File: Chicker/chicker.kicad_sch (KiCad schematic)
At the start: 0 parts

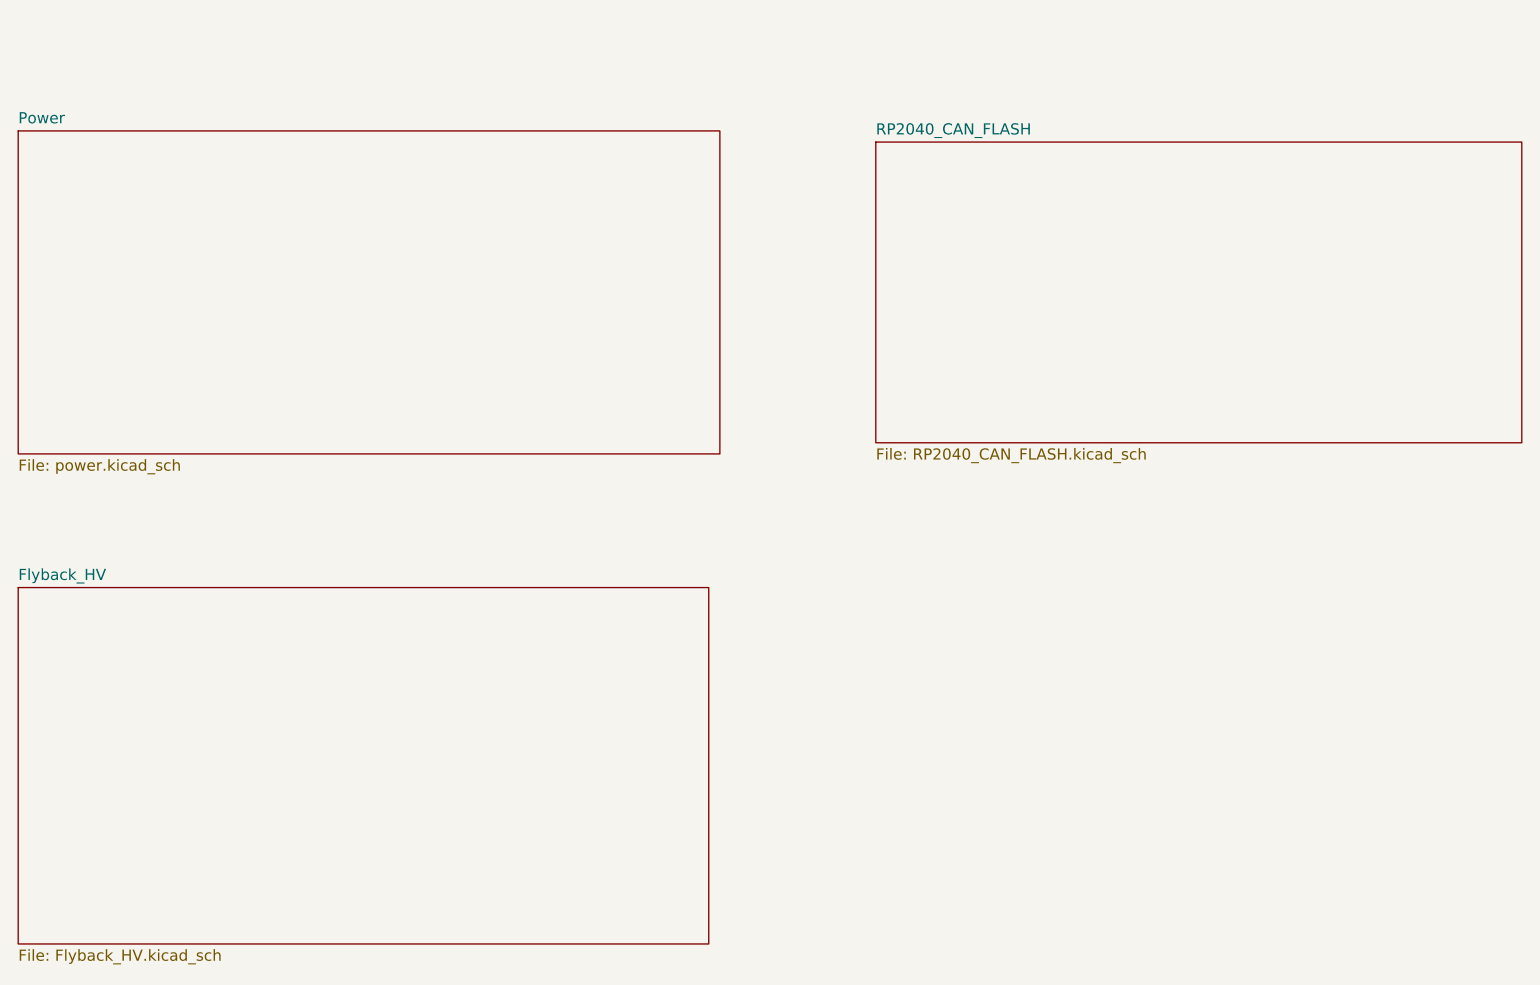
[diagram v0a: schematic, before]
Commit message: update to schematic but something on layout is broken
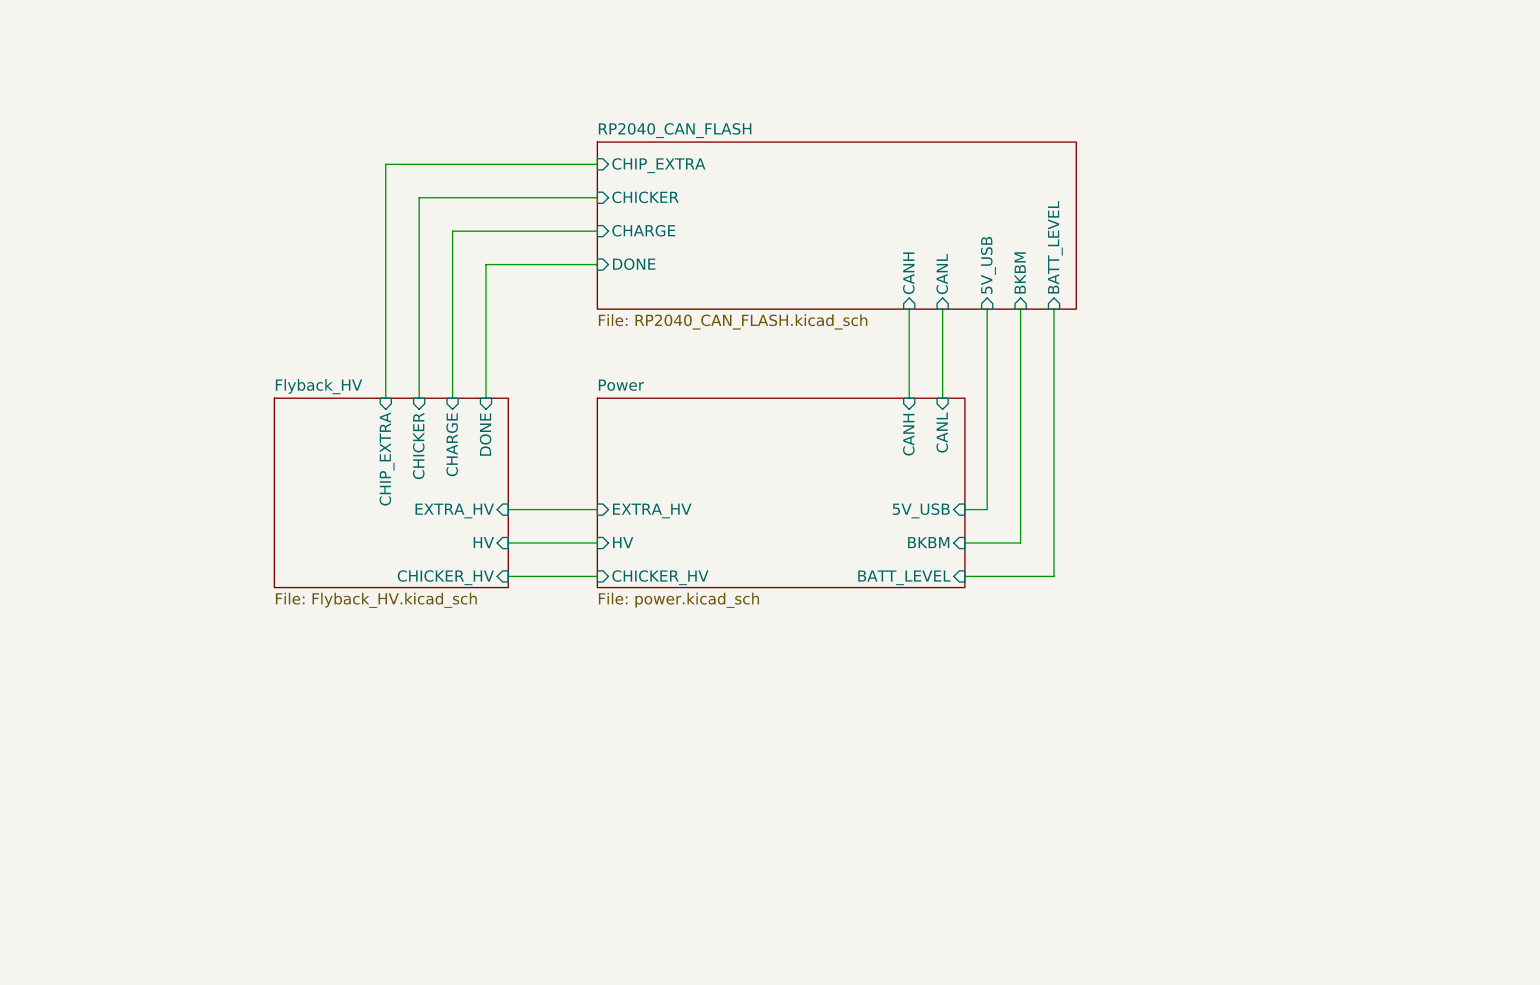
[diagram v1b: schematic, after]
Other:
- sheet Flyback_HV ports: added CHARGE, CHICKER, CHICKER_HV, CHIP_EXTRA, DONE, EXTRA_HV, HV; removed none
- sheet Power ports: added 5V_USB, BATT_LEVEL, BKBM, CANH, CANL, CHICKER_HV, EXTRA_HV, HV; removed none
- sheet RP2040_CAN_FLASH ports: added 5V_USB, BATT_LEVEL, BKBM, CANH, CANL, CHARGE, CHICKER, CHIP_EXTRA, DONE; removed none
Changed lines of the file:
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@@
 (kicad_sch (version 20230121) (generator eeschema)
-  (paper "A4")
-  (sheet (at 31.75 30.48) (size 80.01 36.83) (fields_autoplaced)
+  (paper "A5")
+  (wire (pts (xy 139.7 77.47) (xy 146.05 77.47))
+    (stroke (width 0) (type default))
+  )
+  (wire (pts (xy 142.24 73.66) (xy 139.7 73.66))
+    (stroke (width 0) (type default))
+  )
+  (wire (pts (xy 97.79 38.1) (xy 77.47 38.1))
+    (stroke (width 0) (type default))
+  )
+  (wire (pts (xy 142.24 50.8) (xy 142.24 73.66))
+    (stroke (width 0) (type default))
+  )
+  (wire (pts (xy 149.86 81.28) (xy 149.86 50.8))
+    (stroke (width 0) (type default))
+  )
+  (wire (pts (xy 139.7 81.28) (xy 149.86 81.28))
+    (stroke (width 0) (type default))
+  )
+  (wire (pts (xy 133.35 50.8) (xy 133.35 60.96))
+    (stroke (width 0) (type default))
+  )
+  (wire (pts (xy 87.63 81.28) (xy 97.79 81.28))
+    (stroke (width 0) (type default))
+  )
+  (wire (pts (xy 81.28 41.91) (xy 97.79 41.91))
+    (stroke (width 0) (type default))
+  )
+  (wire (pts (xy 81.28 60.96) (xy 81.28 41.91))
+    (stroke (width 0) (type default))
+  )
+  (wire (pts (xy 97.79 45.72) (xy 85.09 45.72))
+    (stroke (width 0) (type default))
+  )
+  (wire (pts (xy 97.79 34.29) (xy 73.66 34.29))
+    (stroke (width 0) (type default))
+  )
+  (wire (pts (xy 87.63 73.66) (xy 97.79 73.66))
+    (stroke (width 0) (type default))
+  )
+  (wire (pts (xy 87.63 77.47) (xy 97.79 77.47))
+    (stroke (width 0) (type default))
+  )
+  (wire (pts (xy 146.05 77.47) (xy 146.05 50.8))
+    (stroke (width 0) (type default))
+  )
+  (wire (pts (xy 85.09 45.72) (xy 85.09 60.96))
+    (stroke (width 0) (type default))
+  )
+  (wire (pts (xy 137.16 50.8) (xy 137.16 60.96))
+    (stroke (width 0) (type default))
+  )
+  (wire (pts (xy 73.66 34.29) (xy 73.66 60.96))
+    (stroke (width 0) (type default))
+  )
+  (wire (pts (xy 77.47 38.1) (xy 77.47 60.96))
+    (stroke (width 0) (type default))
+  )
+  (sheet (at 97.79 60.96) (size 41.91 21.59) (fields_autoplaced)
     (stroke (width 0.1524) (type solid))
     (fill (color 0 0 0 0.0000))
-    (property "Sheetname" "Power" (at 31.75 29.7684 0)
+    (property "Sheetname" "Power" (at 97.79 60.2484 0)
       (effects (font (size 1.27 1.27)) (justify left bottom))
     )
-    (property "Sheetfile" "power.kicad_sch" (at 31.75 67.8946 0)
+    (property "Sheetfile" "power.kicad_sch" (at 97.79 83.1346 0)
       (effects (font (size 1.27 1.27)) (justify left top))
     )
+    (pin "CANL" input (at 137.16 60.96 90)
+      (effects (font (size 1.27 1.27)) (justify right))
+    )
+    (pin "CHICKER_HV" input (at 97.79 81.28 180)
+      (effects (font (size 1.27 1.27)) (justify left))
+    )
+    (pin "BKBM" input (at 139.7 77.47 0)
+      (effects (font (size 1.27 1.27)) (justify right))
+    )
+    (pin "HV" input (at 97.79 77.47 180)
+      (effects (font (size 1.27 1.27)) (justify left))
+    )
+    (pin "EXTRA_HV" input (at 97.79 73.66 180)
+      (effects (font (size 1.27 1.27)) (justify left))
+    )
+    (pin "CANH" input (at 133.35 60.96 90)
+      (effects (font (size 1.27 1.27)) (justify right))
+    )
+    (pin "5V_USB" input (at 139.7 73.66 0)
+      (effects (font (size 1.27 1.27)) (justify right))
+    )
+    (pin "BATT_LEVEL" input (at 139.7 81.28 0)
+      (effects (font (size 1.27 1.27)) (justify right))
+    )
     (instances
-      (project "POWER_BOARD"
+      (project "chicker"
         (path "/1a9ce3e8-a091-496c-9c5f-e7b2eb60e275" (page "2"))
       )
     )
   )
-  (sheet (at 129.54 31.75) (size 73.66 34.29) (fields_autoplaced)
+  (sheet (at 97.79 31.75) (size 54.61 19.05) (fields_autoplaced)
     (stroke (width 0.1524) (type solid))
     (fill (color 0 0 0 0.0000))
-    (property "Sheetname" "RP2040_CAN_FLASH" (at 129.54 31.0384 0)
+    (property "Sheetname" "RP2040_CAN_FLASH" (at 97.79 31.0384 0)
       (effects (font (size 1.27 1.27)) (justify left bottom))
     )
-    (property "Sheetfile" "RP2040_CAN_FLASH.kicad_sch" (at 129.54 66.6246 0)
+    (property "Sheetfile" "RP2040_CAN_FLASH.kicad_sch" (at 97.79 51.3846 0)
       (effects (font (size 1.27 1.27)) (justify left top))
     )
+    (pin "CANH" input (at 133.35 50.8 270)
+      (effects (font (size 1.27 1.27)) (justify left))
+    )
+    (pin "CANL" input (at 137.16 50.8 270)
+      (effects (font (size 1.27 1.27)) (justify left))
+    )
+    (pin "5V_USB" input (at 142.24 50.8 270)
+      (effects (font (size 1.27 1.27)) (justify left))
+    )
+    (pin "DONE" input (at 97.79 45.72 180)
+      (effects (font (size 1.27 1.27)) (justify left))
+    )
+    (pin "CHICKER" input (at 97.79 38.1 180)
+      (effects (font (size 1.27 1.27)) (justify left))
+    )
+    (pin "CHIP_EXTRA" input (at 97.79 34.29 180)
+      (effects (font (size 1.27 1.27)) (justify left))
+    )
+    (pin "CHARGE" input (at 97.79 41.91 180)
+      (effects (font (size 1.27 1.27)) (justify left))
+    )
+    (pin "BATT_LEVEL" input (at 149.86 50.8 270)
+      (effects (font (size 1.27 1.27)) (justify left))
+    )
+    (pin "BKBM" input (at 146.05 50.8 270)
+      (effects (font (size 1.27 1.27)) (justify left))
+    )
     (instances
-      (project "POWER_BOARD"
+      (project "chicker"
         (path "/1a9ce3e8-a091-496c-9c5f-e7b2eb60e275" (page "3"))
       )
     )
   )
-  (sheet (at 31.75 82.55) (size 78.74 40.64) (fields_autoplaced)
+  (sheet (at 60.96 60.96) (size 26.67 21.59) (fields_autoplaced)
     (stroke (width 0.1524) (type solid))
     (fill (color 0 0 0 0.0000))
-    (property "Sheetname" "Flyback_HV" (at 31.75 81.8384 0)
+    (property "Sheetname" "Flyback_HV" (at 60.96 60.2484 0)
       (effects (font (size 1.27 1.27)) (justify left bottom))
     )
-    (property "Sheetfile" "Flyback_HV.kicad_sch" (at 31.75 123.7746 0)
+    (property "Sheetfile" "Flyback_HV.kicad_sch" (at 60.96 83.1346 0)
       (effects (font (size 1.27 1.27)) (justify left top))
     )
+    (pin "CHICKER" input (at 77.47 60.96 90)
+      (effects (font (size 1.27 1.27)) (justify right))
+    )
+    (pin "CHIP_EXTRA" input (at 73.66 60.96 90)
+      (effects (font (size 1.27 1.27)) (justify right))
+    )
+    (pin "CHARGE" input (at 81.28 60.96 90)
+      (effects (font (size 1.27 1.27)) (justify right))
+    )
+    (pin "DONE" input (at 85.09 60.96 90)
+      (effects (font (size 1.27 1.27)) (justify right))
+    )
+    (pin "HV" input (at 87.63 77.47 0)
+      (effects (font (size 1.27 1.27)) (justify right))
+    )
+    (pin "CHICKER_HV" input (at 87.63 81.28 0)
+      (effects (font (size 1.27 1.27)) (justify right))
+    )
+    (pin "EXTRA_HV" input (at 87.63 73.66 0)
+      (effects (font (size 1.27 1.27)) (justify right))
+    )
     (instances
-      (project "POWER_BOARD"
+      (project "chicker"
         (path "/1a9ce3e8-a091-496c-9c5f-e7b2eb60e275" (page "4"))
       )

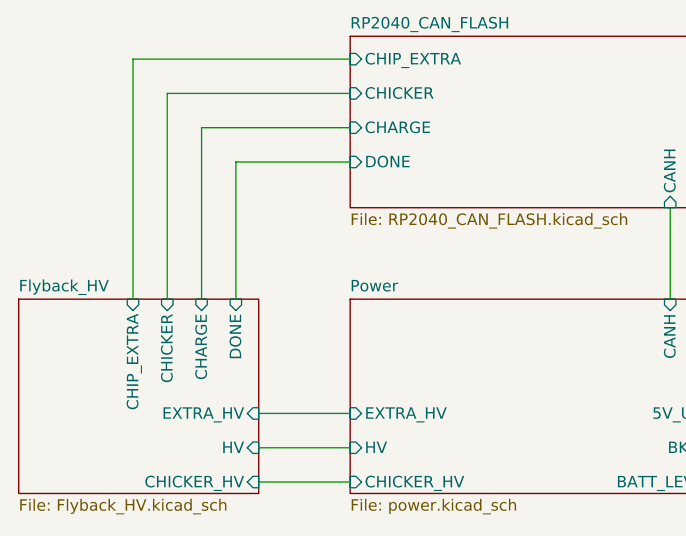
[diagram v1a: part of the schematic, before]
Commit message: midplate 4 layers, chicker shell off limit switch idea
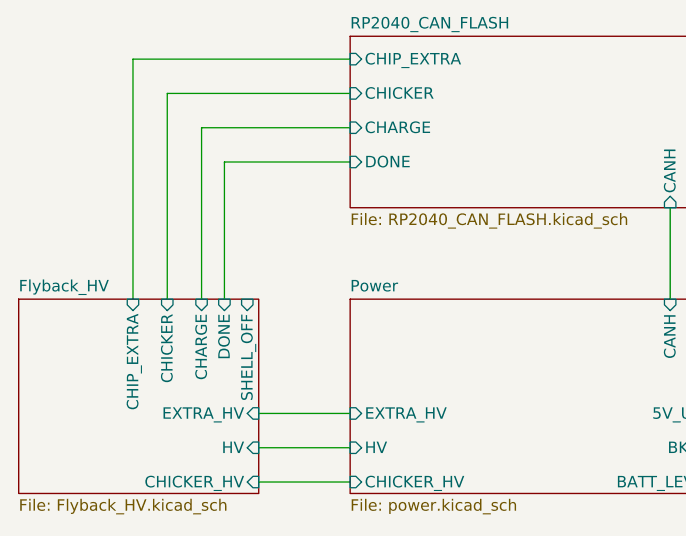
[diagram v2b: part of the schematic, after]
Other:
- sheet Flyback_HV ports: added SHELL_OFF; removed none
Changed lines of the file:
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@@
     (stroke (width 0) (type default))
   )
-  (wire (pts (xy 97.79 45.72) (xy 85.09 45.72))
+  (wire (pts (xy 97.79 45.72) (xy 83.82 45.72))
     (stroke (width 0) (type default))
   )
@@
     (stroke (width 0) (type default))
   )
-  (wire (pts (xy 85.09 45.72) (xy 85.09 60.96))
+  (wire (pts (xy 83.82 45.72) (xy 83.82 60.96))
     (stroke (width 0) (type default))
   )
@@
       (effects (font (size 1.27 1.27)) (justify right))
     )
-    (pin "DONE" input (at 85.09 60.96 90)
+    (pin "DONE" input (at 83.82 60.96 90)
       (effects (font (size 1.27 1.27)) (justify right))
     )
@@
       (effects (font (size 1.27 1.27)) (justify right))
     )
+    (pin "SHELL_OFF" input (at 86.36 60.96 90)
+      (effects (font (size 1.27 1.27)) (justify right))
+    )

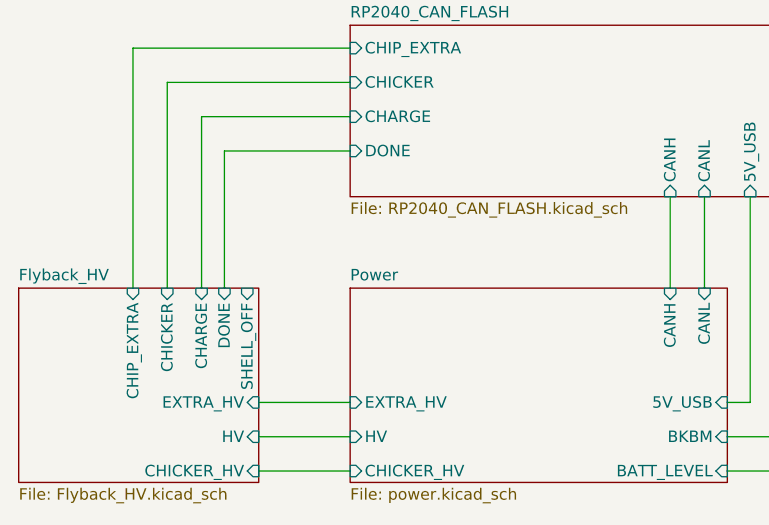
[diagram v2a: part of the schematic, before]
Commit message: chicker discharge HV shell off fixed
pull up to 3v3 and limit switch, input to RP2040, output to inverted discharge signal which discharges if it is set to 0
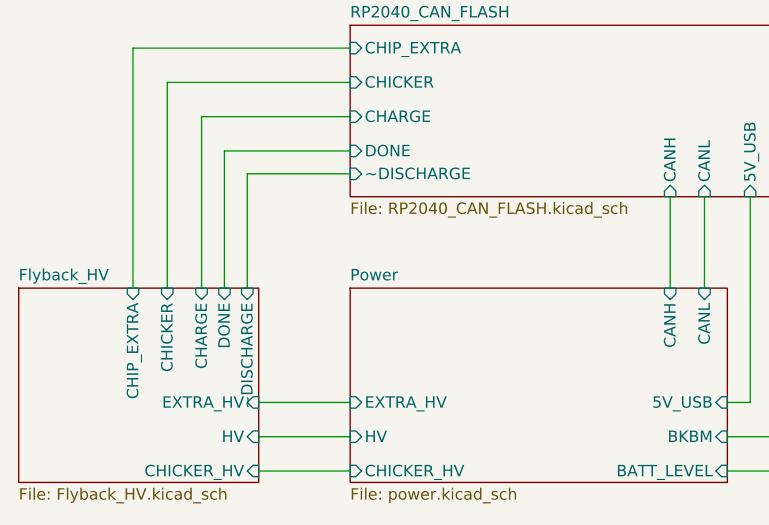
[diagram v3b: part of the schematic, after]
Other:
- sheet Flyback_HV ports: added ~DISCHARGE; removed SHELL_OFF
- sheet RP2040_CAN_FLASH ports: added ~DISCHARGE; removed none
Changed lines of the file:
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@@
+    (stroke (width 0) (type default))
+  )
+  (wire (pts (xy 97.79 48.26) (xy 86.36 48.26))
     (stroke (width 0) (type default))
   )
@@
   )
   (wire (pts (xy 133.35 50.8) (xy 133.35 60.96))
+    (stroke (width 0) (type default))
+  )
+  (wire (pts (xy 86.36 48.26) (xy 86.36 60.96))
     (stroke (width 0) (type default))
   )
@@
       (effects (font (size 1.27 1.27)) (justify left))
     )
+    (pin "~DISCHARGE" input (at 97.79 48.26 180)
+      (effects (font (size 1.27 1.27)) (justify left))
+    )
     (instances
       (project "chicker"
@@
       (effects (font (size 1.27 1.27)) (justify right))
     )
-    (pin "SHELL_OFF" input (at 86.36 60.96 90)
+    (pin "~DISCHARGE" input (at 86.36 60.96 90)
       (effects (font (size 1.27 1.27)) (justify right))
     )
